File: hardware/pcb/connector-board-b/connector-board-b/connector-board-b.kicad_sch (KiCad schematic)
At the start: 4 parts, among them J1 DE9_Pins, J3 Conn_01x02, J4 Conn_01x02, J5 8-215570-0

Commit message: Updated Connectorboard B to rev. 1.1
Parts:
- removed J3: Conn_01x02, TerminalBlock:TerminalBlock_MaiXu_MX126-5.0-02P_1x02_P5.00mm, symbol Connector_Generic:Conn_01x02
- removed J4: Conn_01x02, Connector_JST:JST_EH_B2B-EH-A_1x02_P2.50mm_Vertical, symbol Connector_Generic:Conn_01x02
- added C1, C2: 10u 50V, Capacitor_SMD:C_1210_3225Metric, symbol Device:C
- added C10, C12, C3, C5: 100n, Capacitor_SMD:C_0805_2012Metric, symbol Device:C
- added C11, C8, C9: 10u, Capacitor_SMD:C_1206_3216Metric, symbol Device:C
- added C13: 1n DNP, Capacitor_SMD:C_0805_2012Metric, symbol Device:C
- added C14, C15, C4, C6, C7: 1u, Capacitor_SMD:C_0805_2012Metric, symbol Device:C
- added D1: BAT42W, Diode_SMD:D_SOD-123, symbol Device:D_Schottky
- added D2: CHG (RED), LED_SMD:LED_0805_2012Metric, symbol Device:LED
- added D3: DONE (GRN), LED_SMD:LED_0805_2012Metric, symbol Device:LED
- added F1: PTC 3A (SMD1812P300TF/16), Fuse:Fuse_1812_4532Metric, symbol Device:Polyfuse
- added J2: PANEL_18V, TerminalBlock:TerminalBlock_MaiXu_MX126-5.0-02P_1x02_P5.00mm, symbol Connector:Screw_Terminal_01x02
- added J6: NTC_103AT, Connector_JST:JST_PH_B2B-PH-K_1x02_P2.00mm_Vertical, symbol Connector_Generic:Conn_01x02
- added J7: BATTERY, Connector_JST:JST_EH_B2B-EH-A_1x02_P2.50mm_Vertical, symbol Connector_Generic:Conn_01x02
- added L1: 10u, Inductor_SMD:L_Vishay_IHLP-4040, symbol Device:L
- added Q1, Q2: Si4840BDY, Package_SO:SOIC-8_3.9x4.9mm_P1.27mm, symbol solar_charger:NMOS_SOIC8
- added R1, R3, R4: 499k 1%, Resistor_SMD:R_0805_2012Metric, symbol Device:R
- added R11: 2R2 DNP, Resistor_SMD:R_0805_2012Metric, symbol Device:R
- added R2: 36k 1%, Resistor_SMD:R_0805_2012Metric, symbol Device:R
- added R5: 5k23 1%, Resistor_SMD:R_0805_2012Metric, symbol Device:R
- added R6: 30k1 1%, Resistor_SMD:R_0805_2012Metric, symbol Device:R
- added R7, R8: 2k, Resistor_SMD:R_0805_2012Metric, symbol Device:R
- added RS1, RS3: 0R02 1%, Resistor_SMD:R_1206_3216Metric, symbol Device:R
- added RS2: 0R10 1%, Resistor_SMD:R_1206_3216Metric, symbol Device:R
- added RS4: 0R05 1%, Resistor_SMD:R_1206_3216Metric, symbol Device:R
- added SW1: PWR_KILL, connector-board-b:SW_Toggle_CAX_MTS202C3D1_RightAngle, symbol adapter:SW_DPDT
- added U1: BQ24650RVA, solar_charger:Texas_RVA0016A_VQFN-16-1EP_3.5x3.5mm_P0.5mm_EP2.1x2.1mm, symbol solar_charger:BQ24650RVA
- added U2: INA3221, Package_DFN_QFN:Texas_RGV0016A_VQFN-16-1EP_4x4mm_P0.65mm_EP2.1x2.1mm, symbol Power_Management:INA3221
- added U3: MCP1700-3.3, Package_TO_SOT_SMD:SOT-23, symbol Regulator_Linear:MCP1700x-300xxTT
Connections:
- net GND: now also C1.2, C11.2, C12.2, C13.2, C14.2, C15.2, C2.2, C3.2, C4.2, C6.2, C7.2, C8.2, C9.2, J2.2 (Pin_2), J6.2 (Pin_2), J7.1 (Pin_1), Q2.1 (S), Q2.2 (S), Q2.3 (S), R2.2, R4.2, R6.2, U1.11 (GND), U1.17 (PAD), U2.17 (EP), U2.3 (GND), U3.1 (GND)
- net VCC: now also C10.2, C11.1, C15.1, R3.1, RS1.2, RS3.1, RS4.1, U1.9 (SRN), U2.15 (IN+2), U2.2 (IN+3), U3.3 (VI); no longer J1.2, J5.2
- net LORA_nRESET: now reaches J1.3, J5.3
- net LORA_SWDCLK: now reaches J1.4, J5.4
- net LORA_SWDIO: now reaches J1.5, J5.5
- net LORA_PWR_KILL: now reaches J1.6, J5.6
- net at J1.7: no longer J5.7
- net WALTER_TX: now reaches J1.8, J5.8
- net WALTER_RX: now reaches J1.9, J5.9
- net I2C_SCL: now reaches J5.10
- net I2C_SCL: now also U2.6 (SCL)
- new net: C12.1, C14.1, U2.16 (VPU), U2.4 (VS), U3.2 (VO)
- new net: C10.1, C8.1, C9.1, L1.2, RS1.1, U1.10 (SRP)
- new net: D3.1 (K), U1.5 (STAT2)
- new net: D3.2 (A), R8.2
- new net: C1.1, C2.1, C3.1, C4.1, Q1.5 (D), Q1.6 (D), Q1.7 (D), Q1.8 (D), R1.1, RS2.2, U1.1 (VCC)
- new net: J6.1 (Pin_1), R5.2, R6.1, U1.4 (TS)
- new net: C7.1, R5.1, R7.1, R8.1, U1.6 (VREF), U1.7 (TERM_EN)
- new net: D2.2 (A), R7.2
- new net: R3.2, R4.1, U1.8 (VFB)
- new net: C5.1, D1.1 (K), U1.16 (BTST)
- new net: C5.2, L1.1, Q1.1 (S), Q1.2 (S), Q1.3 (S), Q2.5 (D), Q2.6 (D), Q2.7 (D), Q2.8 (D), R11.1, U1.14 (PH)
- new net: C6.1, D1.2 (A), U1.12 (REGN)
- new net: Q2.4 (G), U1.13 (LODRV)
- new net: Q1.4 (G), U1.15 (HIDRV)
- new net: R1.2, R2.1, U1.2 (MPPSET)
- new net: D2.1 (K), U1.3 (STAT1)
- new net: C13.1, R11.2
- new net BAT+: F1.2, SW1.5 (COM2)
- new net BAT_RAW: J7.2 (Pin_2), SW1.4 (A2)
- new net I2C_SDA: J5.7, U2.5 (A0), U2.7 (SDA)
- new net PANEL+: RS2.1, SW1.2 (COM1), U2.12 (IN+1)
- new net PANEL_RAW: J2.1 (Pin_1), SW1.1 (A1)
- new net VBAT: F1.1, RS3.2, U2.14 (IN-2)
- new net VIN: U2.11 (IN-1)
- new net VLOAD: U2.1 (IN-3)
- new net VLOAD+: J1.2, J5.2, RS4.2
- no-connect marks 0 -> 7
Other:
- note added: "Telemetry always-on from VBAT via U3 (MCP1700, 1.6uA): INA3221 @ 0x42 CH1: Panel CH2: Battery CH3: Load"
- moved on the sheet: J1, J5

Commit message: Cleanup
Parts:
- J5: footprint TwinOak platform footprints:82155700 -> TwinOak:82155700; symbol 8-215570-0:8-215570-0 -> TwinOak:8-215570-0
- SW1: footprint connector-board-b:SW_Toggle_CAX_MTS202C3D1_RightAngle -> TwinOak:SW_Toggle_CAX_MTS202C3D1_RightAngle
- U1: footprint solar_charger:Texas_RVA0016A_VQFN-16-1EP_3.5x3.5mm_P0.5mm_EP2.1x2.1mm -> TwinOak:Texas_RVA0016A_VQFN-16-1EP_3.5x3.5mm_P0.5mm_EP2.1x2.1mm
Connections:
- net VLOAD is gone; now on net VLOAD+: U2.1 (IN-3)
- net VIN: now also C1.1, C2.1, C3.1, C4.1, Q1.5 (D), Q1.6 (D), Q1.7 (D), Q1.8 (D), R1.1, RS2.2, U1.1 (VCC)
- net at D3.1 (K): now also R8.2; no longer U1.5 (STAT2)
- net at D3.2 (A): now also U1.5 (STAT2); no longer R8.2
- net at R7.2: now also D2.1 (K); no longer D2.2 (A)
- net at U1.3 (STAT1): now also D2.2 (A); no longer D2.1 (K)
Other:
- moved on the sheet: D2, D3

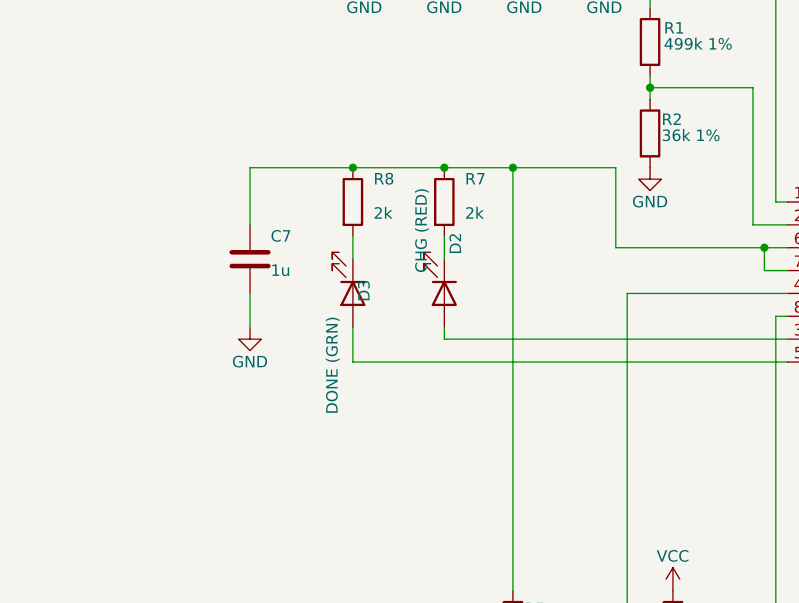
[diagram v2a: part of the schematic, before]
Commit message: Minor connector b updates
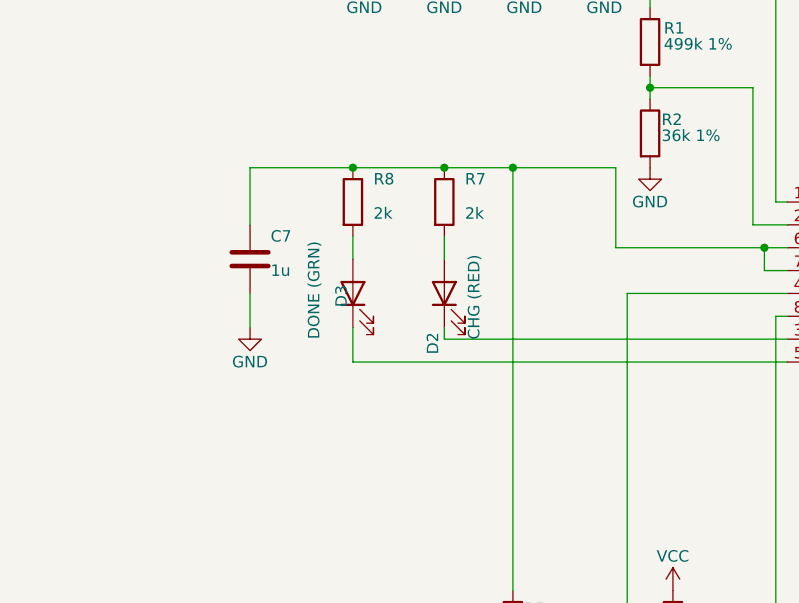
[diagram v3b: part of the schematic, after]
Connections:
- net at D3.1 (K): now also U1.5 (STAT2); no longer R8.2
- net at D3.2 (A): now also R8.2; no longer U1.5 (STAT2)
- net at D2.1 (K): now also U1.3 (STAT1); no longer R7.2
- net at D2.2 (A): now also R7.2; no longer U1.3 (STAT1)

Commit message: Misc changes
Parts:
- added D4: SS54, Diode_SMD:D_SMA, symbol Device:D_Schottky
- added D5: SMBJ26A, Diode_SMD:D_SMB, symbol lora3v3:TVS_V
- L1: LCSC Part # C511353 -> C845066
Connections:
- net GND: now also D5.2
- net PANEL_RAW: now also D4.1 (K); no longer J2.1 (Pin_1)
- new net PANEL_IN: D4.2 (A), D5.1, J2.1 (Pin_1)

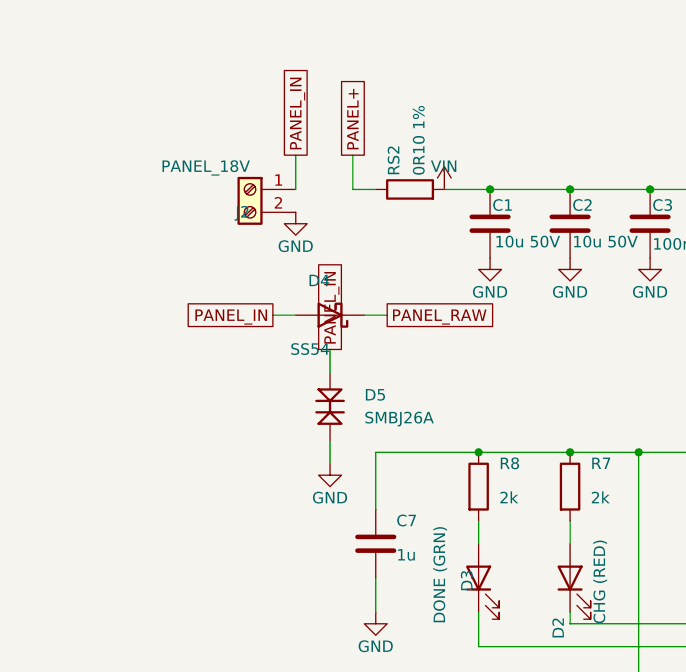
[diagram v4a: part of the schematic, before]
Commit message: Updates according to preflight
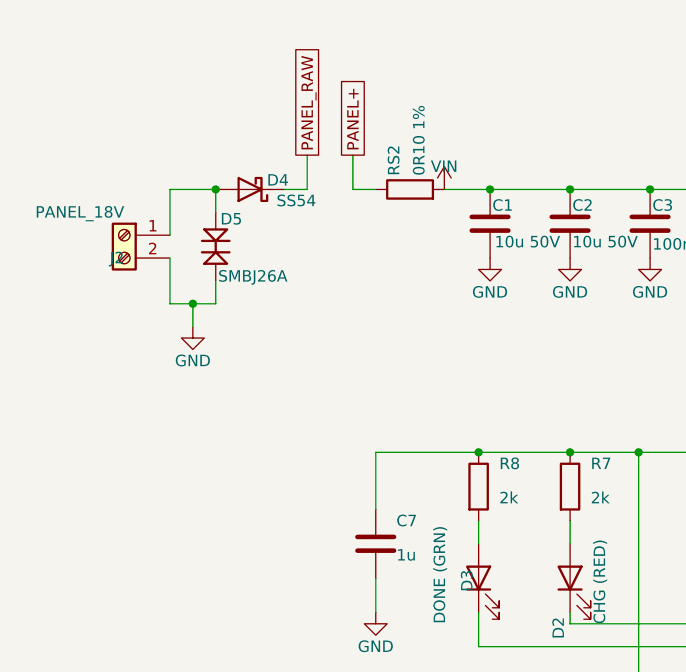
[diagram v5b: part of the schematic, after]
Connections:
- net PANEL_IN: no longer names the net of D4.2 (A), D5.1, J2.1 (Pin_1)
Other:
- moved on the sheet: D5, J2

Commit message: Misc minor updates for production of pcbs
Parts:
- C13, J1, J5, R11: now left out of the parts list
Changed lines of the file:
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@@
 		(body_style 1)
 		(exclude_from_sim no)
-		(in_bom yes)
-		(on_board yes)
-		(in_pos_files yes)
+		(in_bom no)
+		(on_board yes)
+		(in_pos_files no)
 		(dnp yes)
 		(property "Reference" "C13"
@@
 		(body_style 1)
 		(exclude_from_sim no)
-		(in_bom yes)
-		(on_board yes)
-		(in_pos_files yes)
+		(in_bom no)
+		(on_board yes)
+		(in_pos_files no)
 		(dnp no)
 		(fields_autoplaced yes)
@@
 		(body_style 1)
 		(exclude_from_sim no)
-		(in_bom yes)
-		(on_board yes)
-		(in_pos_files yes)
+		(in_bom no)
+		(on_board yes)
+		(in_pos_files no)
 		(dnp no)
 		(fields_autoplaced yes)
@@
 		(body_style 1)
 		(exclude_from_sim no)
-		(in_bom yes)
-		(on_board yes)
-		(in_pos_files yes)
+		(in_bom no)
+		(on_board yes)
+		(in_pos_files no)
 		(dnp yes)
 		(property "Reference" "R11"

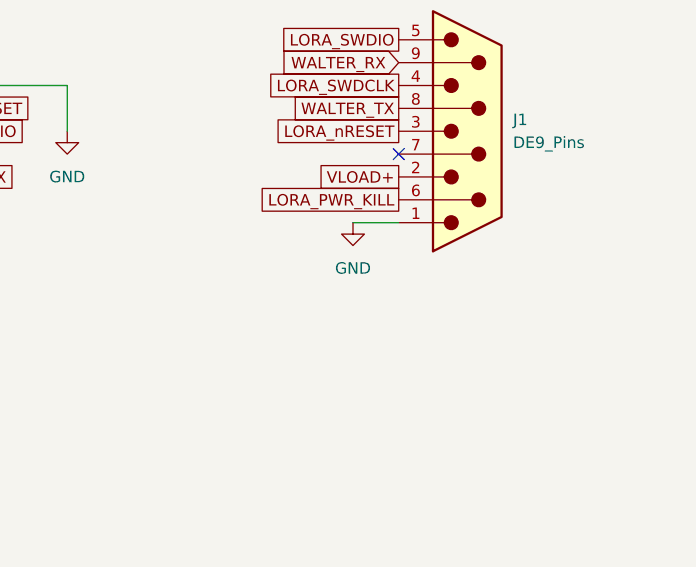
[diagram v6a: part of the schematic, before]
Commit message: Final PCB adjuments to rev 1.1
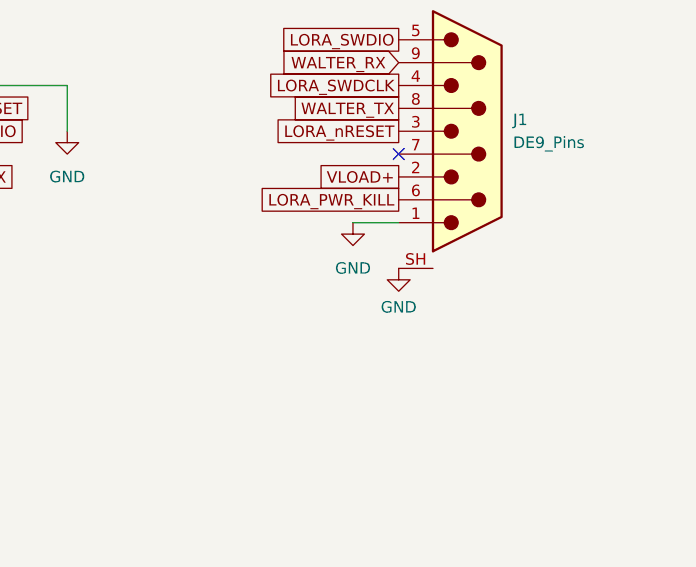
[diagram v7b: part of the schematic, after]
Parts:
- U1: FT Rotation Offset (none) -> -90
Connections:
- net GND: now also J1.SH
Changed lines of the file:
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@@
 			)
 		)
+		(property "FT Rotation Offset" "-90"
+			(at 124.46 93.98 0)
+			(effects
+				(font
+					(size 1.27 1.27)
+				)
+				(hide yes)
+			)
+		)
 		(pin "1"
 		)
@@
 	)
 	(symbol
+		(lib_id "power:GND")
+		(at 342.9 217.17 0)
+		(unit 1)
+		(body_style 1)
+		(exclude_from_sim no)
+		(in_bom yes)
+		(on_board yes)
+		(in_pos_files yes)
+		(dnp no)
+		(property "Reference" "#PWR0211"
+			(at 344.932 215.9 0)
+			(hide yes)
+			(show_name no)
+			(do_not_autoplace no)
+			(effects
+				(font
+					(size 1.27 1.27)
+				)
+			)
+		)
+		(property "Value" "GND"
+			(at 342.9 221.488 0)
+			(show_name no)
+			(do_not_autoplace no)
+			(effects
+				(font
+					(size 1.27 1.27)
+				)
+			)
+		)
+		(property "Footprint" ""
+			(at 342.9 217.17 0)
+			(hide yes)
+			(show_name no)
+			(do_not_autoplace no)
+			(effects
+				(font
+					(size 1.27 1.27)
+				)
+			)
+		)
+		(property "Datasheet" ""
+			(at 342.9 217.17 0)
+			(hide yes)
+			(show_name no)
+			(do_not_autoplace no)
+			(effects
+				(font
+					(size 1.27 1.27)
+				)
+			)
+		)
+		(property "Description" ""
+			(at 342.9 217.17 0)
+			(show_name no)
+			(do_not_autoplace no)
+			(effects
+				(font
+					(size 1.27 1.27)
+				)
+			)
+		)
+		(pin "1"
+		)
+		(instances
+			(project "connector-board-b"
+				(path "/f046fec5-6210-4377-a87a-eb74f5d5b12a"
+					(reference "#PWR0211")
+					(unit 1)
+				)
+			)
+		)
+	)
+	(symbol
 		(lib_id "Connector:DE9_Pins")
 		(at 350.52 201.93 0)
@@
 		(pin "9"
 		)
+		(pin "SH"
+		)
 		(pin "3"

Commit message: Last pre-production updates
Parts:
- J2, J6, J7, SW1: now left out of the parts list
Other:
- moved on the sheet: C1, C10, C11, C12, C13, C14, C15, C2, C3, C4, C5, C6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
